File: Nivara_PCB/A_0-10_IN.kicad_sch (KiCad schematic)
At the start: 5 parts

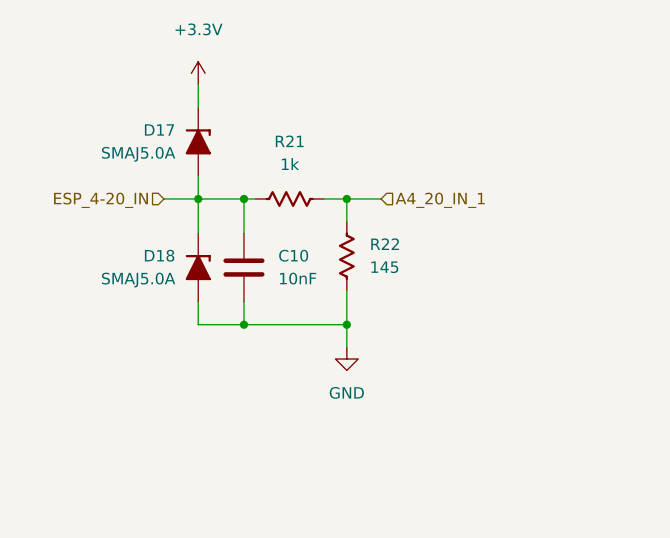
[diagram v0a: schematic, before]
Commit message: Cambios realizados en el PCB y el esquema de Nivara_PCB.
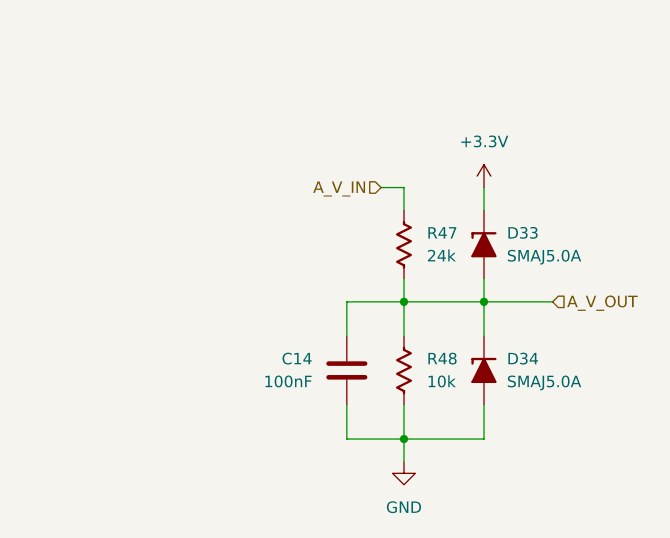
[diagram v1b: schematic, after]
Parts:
- removed C10: 10nF, PCM_Capacitor_SMD_AKL:C_0603_1608Metric, symbol PCM_Capacitor_US_AKL:C_0603
- removed D17, D18: SMAJ5.0A, PCM_Diode_SMD_AKL:D_SMA, symbol PCM_Diode_TVS_AKL:SMAJ5.0A
- removed R21: 1k, PCM_Resistor_SMD_AKL:R_0603_1608Metric, symbol PCM_Resistor_US_AKL:R_0603
- removed R22: 145, PCM_Resistor_SMD_AKL:R_0805_2012Metric, symbol PCM_Resistor_US_AKL:R_0805
- added C14: 100nF, PCM_Capacitor_SMD_AKL:C_0603_1608Metric, symbol PCM_Capacitor_US_AKL:C_0603
- added D33, D34: SMAJ5.0A, PCM_Diode_SMD_AKL:D_SMA, symbol PCM_Diode_TVS_AKL:SMAJ5.0A
- added R47: 24k, PCM_Resistor_SMD_AKL:R_0603_1608Metric, symbol PCM_Resistor_US_AKL:R_0603
- added R48: 10k, PCM_Resistor_SMD_AKL:R_0603_1608Metric, symbol PCM_Resistor_US_AKL:R_0603
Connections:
- net +3.3V: now also D33.1 (K)
- net GND: now also C14.2, D34.2 (A), R48.1
- new net A_V_IN: R47.2
- new net A_V_OUT: C14.1, D33.2 (A), D34.1 (K), R47.1, R48.2

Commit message: Cambios realizados en los archivos de Nivara_PCB.
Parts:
- C14: symbol PCM_Capacitor_US_AKL:C_0603 -> EasyEDA:C_0603
- D33, D34: symbol PCM_Diode_TVS_AKL:SMAJ5.0A -> EasyEDA:SMAJ5.0A
- R47, R48: symbol PCM_Resistor_US_AKL:R_0603 -> EasyEDA:R_0603
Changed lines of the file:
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@@
 	)
 	(symbol
-		(lib_id "power:GND")
+		(lib_id "EasyEDA:GND")
 		(at 78.74 88.9 0)
 		(unit 1)
@@
 	)
 	(symbol
-		(lib_id "PCM_Diode_TVS_AKL:SMAJ5.0A")
+		(lib_id "EasyEDA:SMAJ5.0A")
 		(at 87.63 64.77 90)
 		(unit 1)
@@
 	)
 	(symbol
-		(lib_id "power:+3.3V")
+		(lib_id "EasyEDA:+3.3V")
 		(at 87.63 58.42 0)
 		(unit 1)
@@
 	)
 	(symbol
-		(lib_id "PCM_Diode_TVS_AKL:SMAJ5.0A")
+		(lib_id "EasyEDA:SMAJ5.0A")
 		(at 87.63 78.74 90)
 		(unit 1)
@@
 	)
 	(symbol
-		(lib_id "PCM_Resistor_US_AKL:R_0603")
+		(lib_id "EasyEDA:R_0603")
 		(at 78.74 78.74 180)
 		(unit 1)
@@
 	)
 	(symbol
-		(lib_id "PCM_Resistor_US_AKL:R_0603")
+		(lib_id "EasyEDA:R_0603")
 		(at 78.74 64.77 180)
 		(unit 1)
@@
 	)
 	(symbol
-		(lib_id "PCM_Capacitor_US_AKL:C_0603")
+		(lib_id "EasyEDA:C_0603")
 		(at 72.39 78.74 0)
 		(mirror y)
